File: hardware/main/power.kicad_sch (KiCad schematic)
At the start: 37 parts, among them J1 USB-307HB-B-SU, J2 Conn_01x02, U10 FS8205, U12 USBLC6-2SC6, U5 AP2112K-3.3, U6 AP2112K-3.3, U7 MT3608, U8 BQ24075RGTR, U9 DW01A

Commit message: hardware: pull-ups carte SD, resistances serie d'horloge, timer de charge
Trois points "important" de l'audit 2026-09-23, verifies un par un sur le
schema avant modification (tools/kicad_netlist.py).

H7 — carte SD : aucune pull-up sur J11. L'ESP-IDF les rend obligatoires
(sd_pullup_requirements.rst : « en mode SPI ou SD 1 bit, CMD et DAT0-DAT3
doivent etre tirees au plus par 10k, y compris les lignes non reliees a
l'hote »). Ajout de R15-R19 (10k) sur un rail 3V3_D commun, feuille connector.
DAT1 (J11.8) et DAT2 (J11.1) n'avaient aucun fil : nets nommes SD_DAT1/SD_DAT2.

H8 — horloges SPI : FB1/FB2 (ferrites 120R) remplacees par R13/R14 = 22 ohm
0603. Device:R et Device:FerriteBead ont leurs pins au meme endroit, donc les
fils et la connectivite sont inchanges. Une ferrite sur une horloge rapide
arrondit les fronts et viole les timings de la carte (ESP-IDF sdspi_share.rst,
AC loading) ; les yeux tournent a 40 MHz, 80 visees. Ajout de C6/C7, 10 pF vers
GND en DNP, comme provision jusqu'au test CEM.

H9 — charge LiPo : TMR etait cable directement a GND, c'est-a-dire timers de
securite desactives (bq24075 §6.1). Ajout de R_TMR 56k 1 % entre TMR et GND
-> t_MAXCHG = 10 x K_TMR x R_TMR = 5,6 a 9,3 h (K_TMR 36-60 s/kOhm), pour une
charge de ~4 h a 1 A sur 3000 mAh. Plage admissible datasheet : 18-72 kOhm.

A4 — ICS-43434 sans decouplage : CONSTAT ERRONE, aucune modification faite.
C3 (100 nF 0402, 3V3_A/GND) est deja place a cote de U4 et l'etait deja dans le
fichier du 23/09. Seule subsiste une contrainte de layout (au plus pres des
broches 5 et 3, sans via). Le rapport d'audit et la fiche datasheet sont annotes
en consequence.

tools/kicad_edit.py : helpers d'edition de schema (symboles, fils, labels,
jonctions, remplacement de composant a geometrie de pins identique).
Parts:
- added R_TMR: 56k, Resistor_SMD:R_0402_1005Metric, symbol Device:R
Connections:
- net GND: now also R_TMR.1; no longer U8.14 (TMR)
- new net: R_TMR.2, U8.14 (TMR)
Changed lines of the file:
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@@
 	(wire
 		(pts
-			(xy 176.53 59.69) (xy 185.42 59.69)
-		)
-		(stroke
-			(width 0)
-			(type default)
-		)
-	)
-	(wire
-		(pts
 			(xy 232.41 57.15) (xy 220.98 57.15)
 		)
@@
 		)
 	)
+	(symbol
+		(lib_id "Device:R")
+		(at 180.34 59.69 90)
+		(unit 1)
+		(body_style 1)
+		(exclude_from_sim no)
+		(in_bom yes)
+		(on_board yes)
+		(in_pos_files yes)
+		(dnp no)
+		(property "Reference" "R_TMR"
+			(at 182.88 58.419999999999995 90)
+			(show_name no)
+			(do_not_autoplace no)
+			(effects
+				(font
+					(size 1.27 1.27)
+				)
+			)
+		)
+		(property "Value" "56k"
+			(at 182.88 60.96 90)
+			(show_name no)
+			(do_not_autoplace no)
+			(effects
+				(font
+					(size 1.27 1.27)
+				)
+			)
+		)
+		(property "Footprint" "Resistor_SMD:R_0402_1005Metric"
+			(at 180.34 59.69 90)
+			(hide yes)
+			(show_name no)
+			(do_not_autoplace no)
+			(effects
+				(font
+					(size 1.27 1.27)
+				)
+			)
+		)
+		(property "Datasheet" ""
+			(at 180.34 59.69 0)
+			(hide yes)
+			(show_name no)
+			(do_not_autoplace no)
+			(effects
+				(font
+					(size 1.27 1.27)
+				)
+			)
+		)
+		(property "Description" "Timer de securite bq24075 : 56k -> t_MAXCHG 5,6-9,3 h (10 x K_TMR x R, K_TMR 36-60 s/kOhm). 1 %."
+			(at 180.34 59.69 0)
+			(hide yes)
+			(show_name no)
+			(do_not_autoplace no)
+			(effects
+				(font
+					(size 1.27 1.27)
+				)
+			)
+		)
+		(pin "1"
+		)
+		(pin "2"
+		)
+		(instances
+			(project "blackbox"
+				(path "/49e0257f-ff47-4890-a1ac-89438fa62044/85a32c7c-168b-4c08-8a60-f4e86c1b8173"
+					(reference "R_TMR")
+					(unit 1)
+				)
+			)
+		)
+	)
+	(wire
+		(pts
+			(xy 184.15 59.69) (xy 185.42 59.69)
+		)
+		(stroke
+			(width 0)
+			(type default)
+		)
+	)

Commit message: hardware(power): D1 SS14 -> SS34 (3 A)
Audit 2026-09-23 A5 : le MT3608 est un boost asynchrone, donc tout le courant
du rail 5 V passe par D1. Charge actuelle ~0,83 A (12 WS2812 en blanc 432 mA +
PAM8406 sur 8 ohm ~400 mA), soit juste sous le 1 A du SS14 et sans marge ; le
moindre usage de J9 le depasse. Le SS34 porte la limite a 3 A dans la meme
empreinte SMA pour ~0,013 $.

- Symbole Diode:SS34 derive de Diode:SS14 (memes broches, meme dessin, meme
  empreinte) et embarque dans la feuille : KiCad n'est pas installe dans le
  container, impossible de piocher dans la bibliotheque systeme. Si celle-ci
  n'a pas de symbole SS34, KiCad le signalera a un « Update Symbols from
  Library » — sans effet sur la netlist ni le PCB.
- BOM (les deux copies) : LCSC C8678, MDD SS34, Basic part chez JLCPCB.
- Connexions inchangees, verifiees : anode sur BOOST_SW, cathode sur 5V.

docs/datasheets/SS34.md : deux limites de verification consignees dans la fiche
plutot que passees sous silence — le PDF local est celui de Vishay (famille
SS32-SS36) car LCSC bloque le telechargement de la fiche MDD, et les tableaux
de ce PDF ne sont pas extractibles en texte (la police perd les chiffres). Les
valeurs citees viennent donc des fiches distributeur, marquees comme telles.
SS14.md marquee comme n'etant plus utilisee.
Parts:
- D1: value SS14 -> SS34; symbol Diode:SS14 -> Diode:SS34
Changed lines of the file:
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@@
 	)
 	(symbol
-		(lib_id "Diode:SS14")
+		(lib_id "Diode:SS34")
 		(at 148.59 101.6 180)
 		(unit 1)
@@
 			)
 		)
-		(property "Value" "SS14"
+		(property "Value" "SS34"
 			(at 148.9075 105.41 0)
 			(show_name no)

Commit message: hardware(power): bouton marche/arret (option B) — EN_SYS + load switch 5 V
Audit 2026-09-23 H4 : les EN de U5 (LDO 3V3_D), U6 (LDO 3V3_A) et U7 (boost
MT3608) etaient cables directement sur VSYS, donc la box s'allumait des qu'une
batterie etait branchee — ~10 mA de repos, soit ~12 jours pour 3000 mAh.

Montage (feuille power) :
- net EN_SYS commun aux trois EN, pull-down R20 100k (etat bas garanti si J12
  est ouvert ou debranche), pilote par SW3 (E-Switch 100, contacts or, face
  Cote 2) via J12, JST-SH 2 broches.
- load switch Q1 (AO3401A) sur le rail 5 V, commande par Q2 (2N7002) + R21
  100k. Il est indispensable : le MT3608 est un boost asynchrone, EN bas laisse
  passer VBAT par L1 + D1 et les 12 WS2812 resteraient alimentees.
- Q2 inverse parce qu'un P-MOS high-side conduit grille basse alors que EN_SYS
  est haut box allumee. Marge verifiee : EN_SYS = VSYS, soit 3,0 V au pire
  (batterie en fin de decharge) contre un V_GS(th) de 2,0 V max (datasheet).
- orientation de Q1 verifiee : Source cote boost, Drain cote charge. La diode
  intrinseque va du Drain vers la Source ; box eteinte, source a VBAT - V_F et
  drain a 0 V, donc bloquee. Inversee, elle aurait rendu le switch inutile.
- le rail est coupe en deux : 5V_BOOST (D1, C_B2 et le feedback R_FB_H, qui
  reste cote boost) et 5V (12 WS2812, PAM8406, J9). Chute ~50 mV a 0,83 A avec
  R_DS(ON) 60 mOhm, la charge voit ~5,05 V.

Verifie par netlist : EN_SYS porte bien les 6 pins attendues, VSYS n'a plus
aucun EN, GATE_5V relie Q1.G / Q2.D / R21.

Symboles Transistor_FET:AO3401A et 2N7002 repris de la bibliotheque KiCad
officielle (v9) et aplatis comme le fait KiCad a l'enregistrement — plutot que
redessines, pour qu'un « Update Symbols from Library » ne deplace pas les
broches. Brochage SOT-23 1=G, 2=S, 3=D.

BOM (les deux copies) : Q1 C15127, Q2 C8545, R20/R21, J12, SW3.
Fiches : AO3401A.md, 2N7002.md (+ PDF). Celle du 2N7002 signale que le PDF est
de Diodes alors que le composant LCSC est de JSCJ — sans conse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
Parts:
- added J12: Interrupteur, Connector_JST:JST_SH_BM02B-SRSS-TB_1x02-1MP_P1.00mm_Vertical, symbol Connector_Generic:Conn_01x02
- added Q1: AO3401A, Package_TO_SOT_SMD:SOT-23, symbol Transistor_FET:AO3401A
- added Q2: 2N7002, Package_TO_SOT_SMD:SOT-23, symbol Transistor_FET:2N7002
- added R20, R21: 100k, Resistor_SMD:R_0402_1005Metric, symbol Device:R
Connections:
- net 5V: now also Q1.3 (D); no longer C_B2.1, D1.1 (K), R_FB_H.1
- net GND: now also Q2.2 (S), R20.2
- net VSYS: now also J12.1 (Pin_1); no longer L1.1, U5.3 (EN), U6.3 (EN), U7.4 (EN)
- new net 5V_BOOST: C_B2.1, D1.1 (K), Q1.2 (S), R21.1, R_FB_H.1
- new net EN_SYS: J12.2 (Pin_2), Q2.1 (G), R20.1, U5.3 (EN), U6.3 (EN), U7.4 (EN)
- new net GATE_5V: Q1.1 (G), Q2.3 (D), R21.2

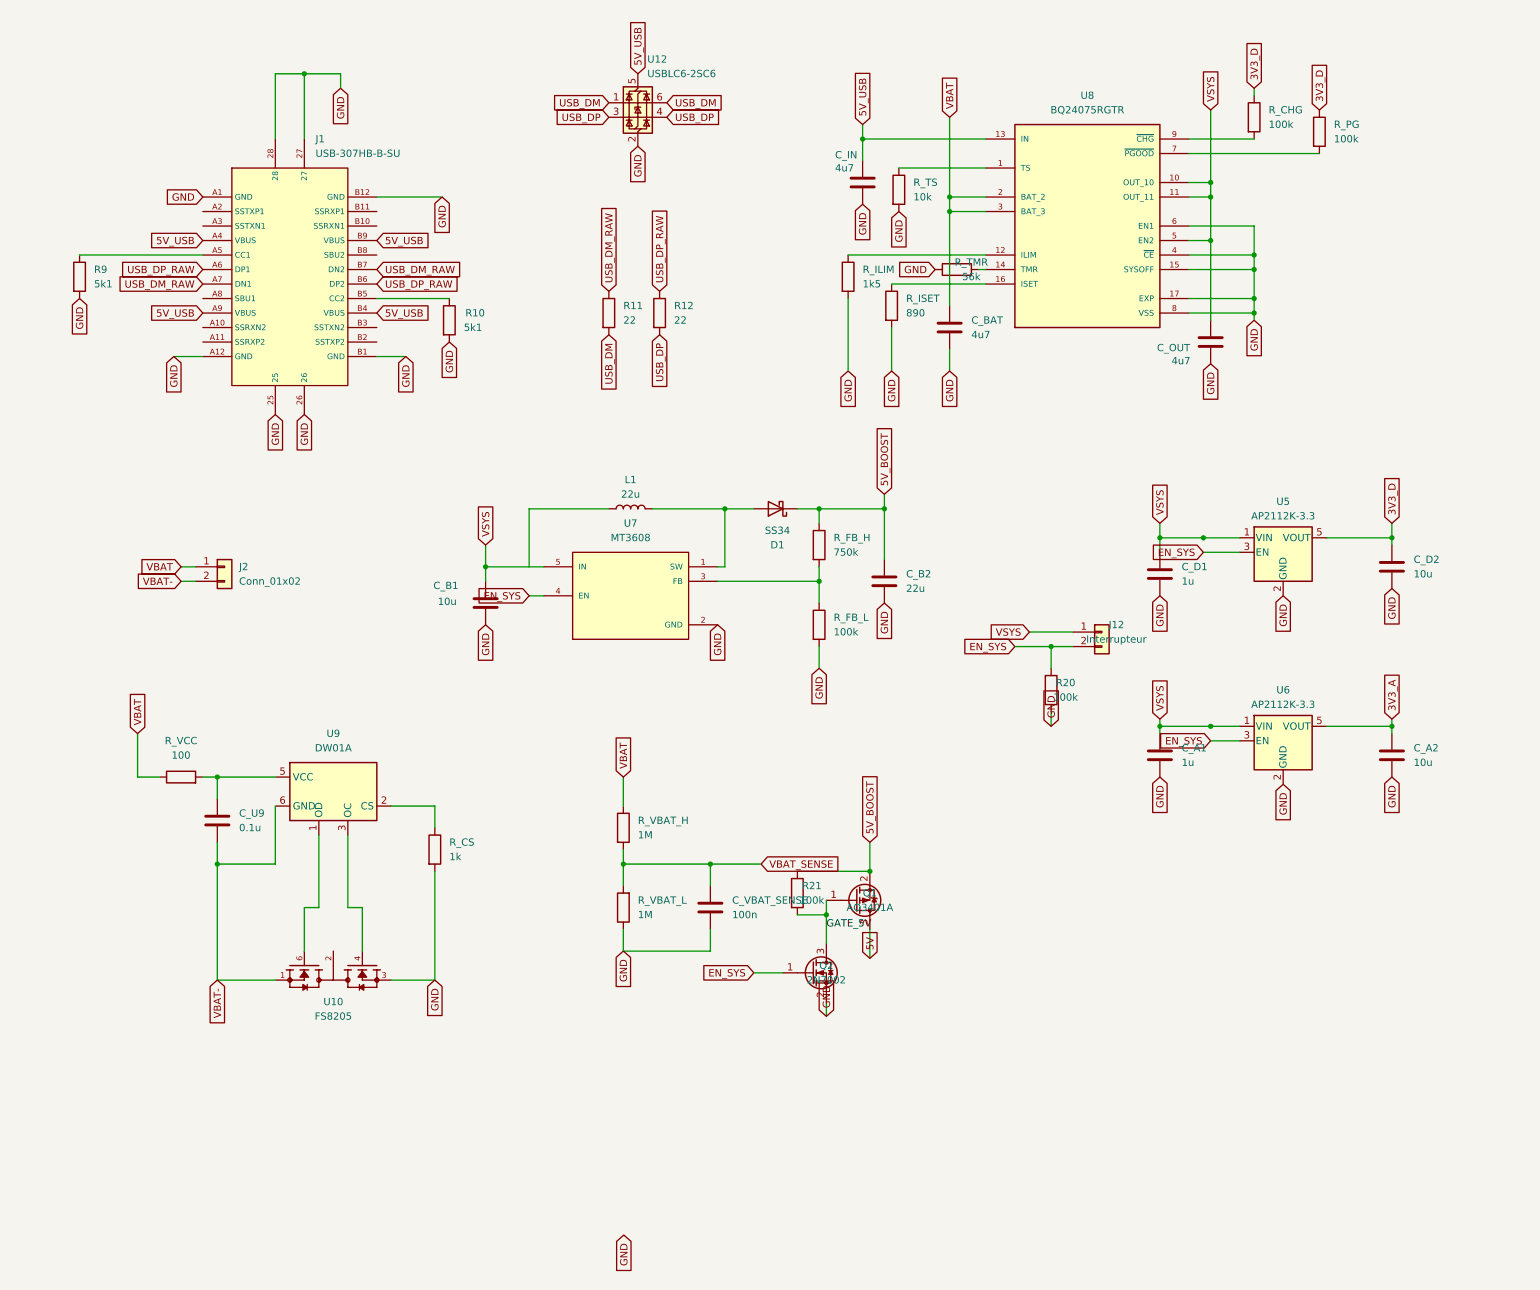
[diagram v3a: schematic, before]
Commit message: hardware(power): U5 (3V3_D) en SO-8 — AP2112M-3.3TRG1
Audit 2026-09-23 H5 : en SOT-25 (theta JA 184 C/W), U5 dissipe 0,56 W sous USB
a 400 mA, soit +103 C d'elevation en boitier ferme. Le SO-8 (114 C/W) ramene
l'elevation a +64 C — meilleur que le SOT-89-5 envisage dans l'audit (120 C/W),
et surtout disponible chez LCSC (C5290219), ce que n'etait pas le SOT-89-5.

U6 (3V3_A) reste en SOT-25 : il n'alimente que le PCM5122, ~25 mA, il ne
chauffe pas. Deux references du meme LDO dans la BOM, assume.

Brochage SO-8 releve sur le dessin de la datasheet (le tableau correspondant
n'est pas extractible en texte, et les sources web se contredisaient) :
1 = VOUT, 2/3/4 = NC, 5 = EN, 6+7 = GND, 8 = VIN. Il n'a rien de commun avec
celui du SOT-25 (1 = VIN, 2 = GND, 3 = EN, 5 = VOUT).

Symbole : la bibliotheque KiCad officielle ne contient que les variantes K
(SOT-25), le symbole a donc ete cree dans la bibliotheque projet
`lcsc_imported`, avec les positions de broches du symbole officiel — VIN, EN et
VOUT retombent ainsi exactement sur les fils deja en place. Seules les deux
masses (6 et 7) ont demande un fil, et le global label GND existant se trouvait
deja pile entre elles.

Verifie par netlist : VIN->VSYS, EN->EN_SYS, VOUT->3V3_D, GND sur les deux
broches, 3V3_D intact avec ses 28 consommateurs, U6 inchange.

Reste a faire au layout : plan de cuivre genereux sous et autour de U5.
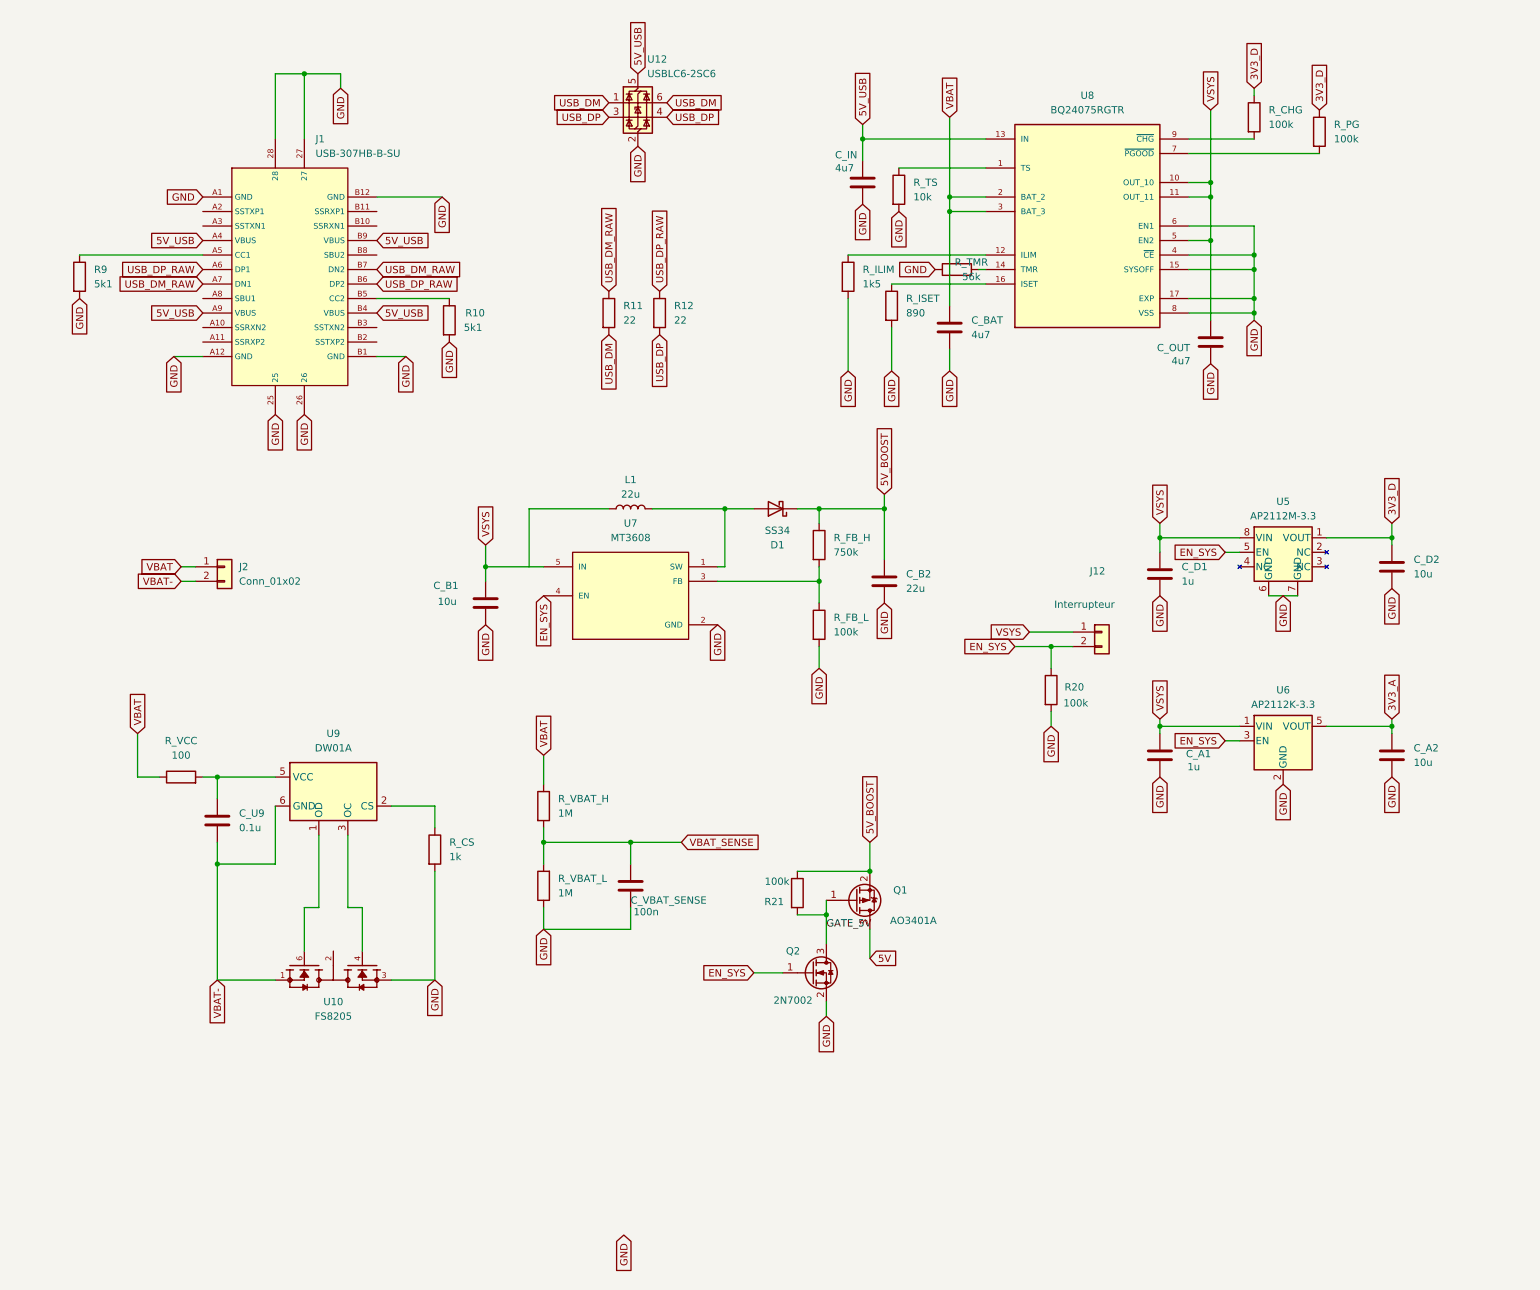
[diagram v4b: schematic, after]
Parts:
- U5: value AP2112K-3.3 -> AP2112M-3.3; footprint Package_TO_SOT_SMD:SOT-23-5 -> Package_SO:SOIC-8_3.9x4.9mm_P1.27mm; symbol Regulator_Linear:AP2112K-3.3 -> lcsc_imported:AP2112M-3.3
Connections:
- net 3V3_D: now also U5.1 (VOUT); no longer U5.5 (VOUT)
- net EN_SYS: now also U5.5 (EN); no longer U5.3 (EN)
- net GND: now also U5.6 (GND), U5.7 (GND); no longer U5.2 (GND)
- net VSYS: now also U5.8 (VIN); no longer U5.1 (VIN)
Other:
- moved on the sheet: C_VBAT_SENSE, R_VBAT_H, R_VBAT_L

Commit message: hardware(power): corrections issues de l'ERC — jonction L1 et empreintes JST
Deux points remontes par l'ERC du 2026-09-27 (0 erreur, 148 warnings).

1. REGRESSION de ma part, corrigee : en isolant l'EN de U7 pour le net EN_SYS,
   j'avais aussi supprime la jonction (105.41, 111.76) en la croyant devenue
   inutile. Elle portait en realite une seconde derivation : VSYS -> L1,
   l'inductance du boost. Sans elle, KiCad signalait une extremite de fil non
   connectee — autrement dit le MT3608 n'etait plus alimente. Jonction
   retablie, L1.1 de nouveau sur VSYS (verifie par netlist).
   Lecon : une jonction peut porter plus de branches que celle qu'on retire ;
   verifier ce qui passe par le point avant de la supprimer.

2. Empreintes JST PH introuvables (J2, J9, J10) : le projet utilisait
   « ...1x02-P2.00mm... » alors que la bibliotheque KiCad nomme
   « ...1x02_P2.00mm... » (underscore et non tiret). Defaut preexistant sur J2
   et J9, que j'avais propage a J10 en copiant J9. Les trois noms sont
   corriges et verifies contre la bibliotheque officielle, de meme que toutes
   les empreintes ajoutees depuis (SOIC-8, SOT-23, L_0805, R_0603, R_0402,
   C_0402, JST_SH 1x02).
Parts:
- J2: footprint Connector_JST:JST_PH_B2B-PH-K_1x02-P2.00mm_Vertical -> Connector_JST:JST_PH_B2B-PH-K_1x02_P2.00mm_Vertical
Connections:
- net VSYS: now also L1.1
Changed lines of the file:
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@@
 			)
 		)
-		(property "Footprint" "Connector_JST:JST_PH_B2B-PH-K_1x02-P2.00mm_Vertical"
+		(property "Footprint" "Connector_JST:JST_PH_B2B-PH-K_1x02_P2.00mm_Vertical"
 			(at 52.07 111.76 0)
 			(hide yes)
@@
 		)
 	)
+	(junction
+		(at 105.41 111.76)
+		(diameter 0)
+		(color 0 0 0 0)
+	)
 )
